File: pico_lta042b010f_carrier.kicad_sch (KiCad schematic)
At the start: 25 parts, among them J1 LTA042B010F_FFC36, J2 USB-C 5V INPUT, J3 13V8 OUT, U1 RaspberryPi_Pico_2W, U3 MC34063AD

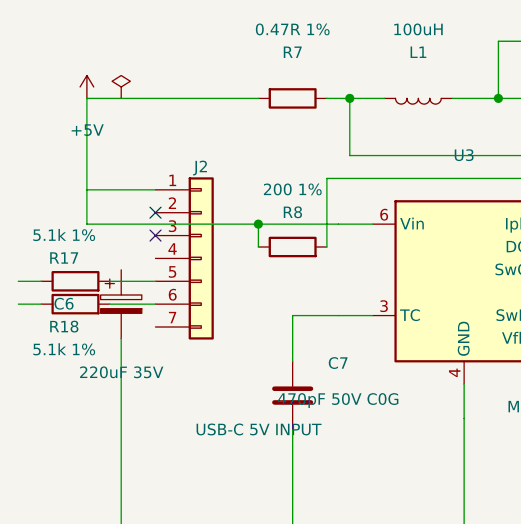
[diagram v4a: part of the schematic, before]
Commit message: Use compact Akizuki USB-C power connector
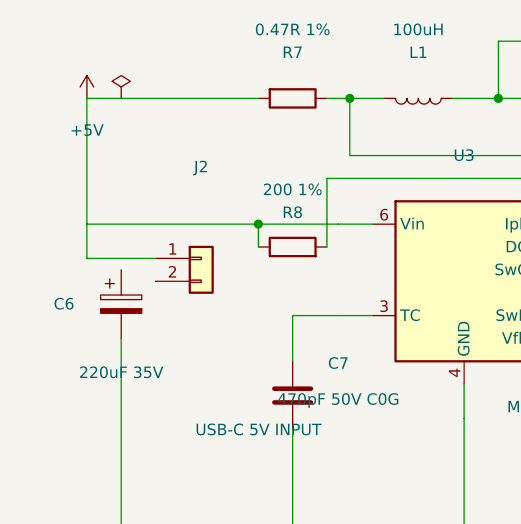
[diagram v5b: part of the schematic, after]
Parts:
- removed R17, R18: 5.1k 1%, Resistor_THT:R_Axial_DIN0204_L3.6mm_D1.6mm_P2.54mm_Vertical, symbol Device:R
- J2: footprint Custom:AE_USB2.0_TYPE_C -> Custom:A295_CTRPB_1; symbol Connector_Generic:Conn_01x07 -> Connector_Generic:Conn_01x02; AkizukiCode 113080 -> 116895; MPN AE-USB2.0-TYPE-C -> A295-CTRPB-1; Manufacturer Akizuki Denshi Tsusho -> Chang Enn Co., Ltd.; SelectionNote USB Type-C female breakout; seven 2.54mm through-hole pins;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 -> compact power-only USB Type-C receptacle; through-hole; no 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; SourceURL https://akizukidenshi.com/catalog/g/g113080/ -> https://akizukidenshi.com/catalog/g/g116895/
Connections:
- net GND: now also J2.2 (Pin_2); no longer J2.4 (Pin_4), J2.7 (Pin_7)
- removed net USB_CC1: J2.5 (Pin_5)
- removed net USB_CC2: J2.6 (Pin_6)
- no-connect marks 11 -> 9
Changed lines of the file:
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@@
 		(instances (project "pico_lta042b010f_carrier" (path "/10000000-0000-4000-8000-000000000001" (reference "J1") (unit 1))))
 	)
-(symbol (lib_id "Connector_Generic:Conn_01x07") (at 78.74 39.37 0) (unit 1)
+(symbol (lib_id "Connector_Generic:Conn_01x02") (at 78.74 39.37 0) (unit 1)
 		(exclude_from_sim no) (in_bom yes) (on_board yes) (dnp no)
 		(property "Reference" "J2" (at 78.74 29.21 0) (effects (font (size 1.27 1.27))))
 		(property "Value" "USB-C 5V INPUT" (at 85.09 58.42 0) (effects (font (size 1.27 1.27))))
-		(property "Footprint" "Custom:AE_USB2.0_TYPE_C" (at 0 0 0) (effects (font (size 1.27 1.27)) hide))
+		(property "Footprint" "Custom:A295_CTRPB_1" (at 0 0 0) (effects (font (size 1.27 1.27)) hide))
 		(property "Datasheet" "" (at 0 0 0) (effects (font (size 1.27 1.27)) hide))
-		(property "Manufacturer" "Akizuki Denshi Tsusho" (at 0 0 0) (effects (font (size 1.27 1.27)) hide))
-		(property "MPN" "AE-USB2.0-TYPE-C" (at 0 0 0) (effects (font (size 1.27 1.27)) hide))
-		(property "AkizukiCode" "113080" (at 0 0 0) (effects (font (size 1.27 1.27)) hide))
-		(property "Supplier" "Akizuki Denshi" (at 0 0 0) (effects (font (size 1.27 1.27)) hide))
-		(property "SourceURL" "https://akizukidenshi.com/catalog/g/g113080/" (at 0 0 0) (effects (font (size 1.27 1.27)) hide))
-		(property "SelectionNote" "USB Type-C female breakout; seven 2.54mm through-hole pins; CC1/CC2 each require 5.1kohm to GND" (at 0 0 0) (effects (font (size 1.27 1.27)) hide))
+		(property "Manufacturer" "Chang Enn Co., Ltd." (at 0 0 0) (effects (font (size 1.27 1.27)) hide))
+		(property "MPN" "A295-CTRPB-1" (at 0 0 0) (effects (font (size 1.27 1.27)) hide))
+		(property "AkizukiCode" "116895" (at 0 0 0) (effects (font (size 1.27 1.27)) hide))
+		(property "Supplier" "Akizuki Denshi" (at 0 0 0) (effects (font (size 1.27 1.27)) hide))
+		(property "SourceURL" "https://akizukidenshi.com/catalog/g/g116895/" (at 0 0 0) (effects (font (size 1.27 1.27)) hide))
+		(property "SelectionNote" "compact power-only USB Type-C receptacle; through-hole; no CC contacts; use a USB-A source with an A-to-C cable" (at 0 0 0) (effects (font (size 1.27 1.27)) hide))
 		(property "Description" "5V input for the on-board MC34063 bipolar supply" (at 0 0 0) (effects (font (size 1.27 1.27)) hide))
 		(pin "1")
 		(pin "2")
-				(pin "3")
-		(pin "4")
-		(pin "5")
-		(pin "6")
-		(pin "7")
 (instances (project "pico_lta042b010f_carrier" (path "/10000000-0000-4000-8000-000000000001" (reference "J2") (unit 1))))
 	)
@@
 		(pin "3")
 		(instances (project "pico_lta042b010f_carrier" (path "/10000000-0000-4000-8000-000000000001" (reference "RV1") (unit 1))))
-	)
-(symbol (lib_id "Device:R") (at 64.77 41.91 90) (unit 1)
-		(exclude_from_sim no) (in_bom yes) (on_board yes) (dnp no)
-		(property "Reference" "R17" (at 63.5 39.37 270) (effects (font (size 1.27 1.27))))
-		(property "Value" "5.1k 1%" (at 63.5 36.83 270) (effects (font (size 1.27 1.27))))
-		(property "Footprint" "Resistor_THT:R_Axial_DIN0204_L3.6mm_D1.6mm_P2.54mm_Vertical" (at 0 0 0) (effects (font (size 1.27 1.27)) hide))		(property "Manufacturer" "FAITHFUL LINK INDUSTRIAL CORP." (at 0 0 0) (effects (font (size 1.27 1.27)) hide))
-		(property "MPN" "MFS25F5K1B" (at 0 0 0) (effects (font (size 1.27 1.27)) hide))
-		(property "AkizukiCode" "108547" (at 0 0 0) (effects (font (size 1.27 1.27)) hide))
-		(property "Supplier" "Akizuki Denshi" (at 0 0 0) (effects (font (size 1.27 1.27)) hide))
-		(property "SourceURL" "https://akizukidenshi.com/catalog/g/g108547/" (at 0 0 0) (effects (font (size 1.27 1.27)) hide))
-		(property "SelectionNote" "5.1kohm +/-1%; USB Type-C CC1 pull-down; vertical mounting" (at 0 0 0) (effects (font (size 1.27 1.27)) hide))
-		(pin "1")
-		(pin "2")
-		(instances (project "pico_lta042b010f_carrier" (path "/10000000-0000-4000-8000-000000000001" (reference "R17") (unit 1))))
-	)
-(symbol (lib_id "Device:R") (at 64.77 44.45 90) (unit 1)
-		(exclude_from_sim no) (in_bom yes) (on_board yes) (dnp no)
-		(property "Reference" "R18" (at 63.5 46.99 270) (effects (font (size 1.27 1.27))))
-		(property "Value" "5.1k 1%" (at 63.5 49.53 270) (effects (font (size 1.27 1.27))))
-		(property "Footprint" "Resistor_THT:R_Axial_DIN0204_L3.6mm_D1.6mm_P2.54mm_Vertical" (at 0 0 0) (effects (font (size 1.27 1.27)) hide))		(property "Manufacturer" "FAITHFUL LINK INDUSTRIAL CORP." (at 0 0 0) (effects (font (size 1.27 1.27)) hide))
-		(property "MPN" "MFS25F5K1B" (at 0 0 0) (effects (font (size 1.27 1.27)) hide))
-		(property "AkizukiCode" "108547" (at 0 0 0) (effects (font (size 1.27 1.27)) hide))
-		(property "Supplier" "Akizuki Denshi" (at 0 0 0) (effects (font (size 1.27 1.27)) hide))
-		(property "SourceURL" "https://akizukidenshi.com/catalog/g/g108547/" (at 0 0 0) (effects (font (size 1.27 1.27)) hide))
-		(property "SelectionNote" "5.1kohm +/-1%; USB Type-C CC2 pull-down; vertical mounting" (at 0 0 0) (effects (font (size 1.27 1.27)) hide))
-		(pin "1")
-		(pin "2")
-		(instances (project "pico_lta042b010f_carrier" (path "/10000000-0000-4000-8000-000000000001" (reference "R18") (unit 1))))
 	)
 (no_connect (at 110.49 132.08))
@@
 	(wire
 		(pts
-			(xy 73.66 31.75) (xy 66.04 31.75)
-		)
-		(stroke (width 0) (type solid))
-	)
-	(wire
-		(pts
-			(xy 66.04 31.75) (xy 66.04 21.59)
-		)
-		(stroke (width 0) (type solid))
-	)
-	(wire
-		(pts
-			(xy 66.04 31.75) (xy 66.04 35.56)
+			(xy 73.66 39.37) (xy 66.04 39.37)
+		)
+		(stroke (width 0) (type solid))
+	)
+	(wire
+		(pts
+			(xy 66.04 39.37) (xy 66.04 35.56)
+		)
+		(stroke (width 0) (type solid))
+	)
+	(wire
+		(pts
+			(xy 66.04 35.56) (xy 66.04 21.59)
 		)
 		(stroke (width 0) (type solid))
@@
 	(wire
 		(pts
-			(xy 73.66 41.91) (xy 68.58 41.91)
-		)
-		(stroke (width 0) (type solid))
-	)
-	(wire
-		(pts
-			(xy 60.96 41.91) (xy 58.42 41.91)
-		)
-		(stroke (width 0) (type solid))
-	)
-	(wire
-		(pts
-			(xy 73.66 44.45) (xy 68.58 44.45)
-		)
-		(stroke (width 0) (type solid))
-	)
-	(wire
-		(pts
-			(xy 60.96 44.45) (xy 58.42 44.45)
-		)
-		(stroke (width 0) (type solid))
-	)
-	(wire
-		(pts
 			(xy 66.04 35.56) (xy 93.98 35.56)
 		)
@@
 		)
 		(stroke (width 0) (type solid))
-	)
-	(no_connect
-		(at 73.66 34.29)
-	)
-	(no_connect
-		(at 73.66 36.83)
 	)
 	(junction
@@
 	)
 	(label "GND"
-		(at 73.66 39.37 0)
-		(effects (font (size 0.01 0.01)) (hide yes))
-	)
-	(label "USB_CC1"
 		(at 73.66 41.91 0)
 		(effects (font (size 0.01 0.01)) (hide yes))
 	)
-	(label "USB_CC2"
-		(at 73.66 44.45 0)
-		(effects (font (size 0.01 0.01)) (hide yes))
-	)
-	(label "GND"
-		(at 73.66 46.99 0)
-		(effects (font (size 0.01 0.01)) (hide yes))
-	)
-	(label "GND"
-		(at 58.42 41.91 180)
-		(effects (font (size 0.01 0.01)) (hide yes))
-	)
-	(label "GND"
-		(at 58.42 44.45 180)
-		(effects (font (size 0.01 0.01)) (hide yes))
-	)
